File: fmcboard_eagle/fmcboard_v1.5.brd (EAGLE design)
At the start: 147 x 74 mm, 176 parts, among them IC1 OPA699ID, IC10 LTC6229IMS8E#TRPBF, IC11 7805TV, IC12 SN74AUC2G66DCTR, IC13 SN74AUC2G66DCTR, IC14 SN74AUC2G66DCTR, IC15 SN74AUC2G66DCTR, IC16 DAC7578SPWR, IC17 SN74AUC2G66DCTR, IC18 SN74AUC2G66DCTR, IC19 SN74AUC2G66DCTR, IC2 DAC7578SPWR, IC20 SN74AUC2G66DCTR, IC21 74AUP2GU04GW,125, IC22 74AUP2GU04GW,125, IC23 74AUP2GU04GW,125, IC24 74AUP2GU04GW,125, IC25 LM358, IC3 LTC6229IMS8E#TRPBF, IC4 LTC6229IMS8E#TRPBF, IC6 OPA699ID, IC7 OPA699ID, IC8 LTC6229IMS8E#TRPBF, IC9 LTC6229IMS8E#TRPBF, J1 8pin, J10 8pin, J12 4p-2.54, J2 ASP-134604-01, J3 4p-2.54, J4 4p-2.54, J5 8pin, J6 4p-2.54, J7 4p-2.54, J8 4p-2.54, J9 8pin, U1 TXS0108EPWR, U2 STMICROELECTRONICS_L7905ACVST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

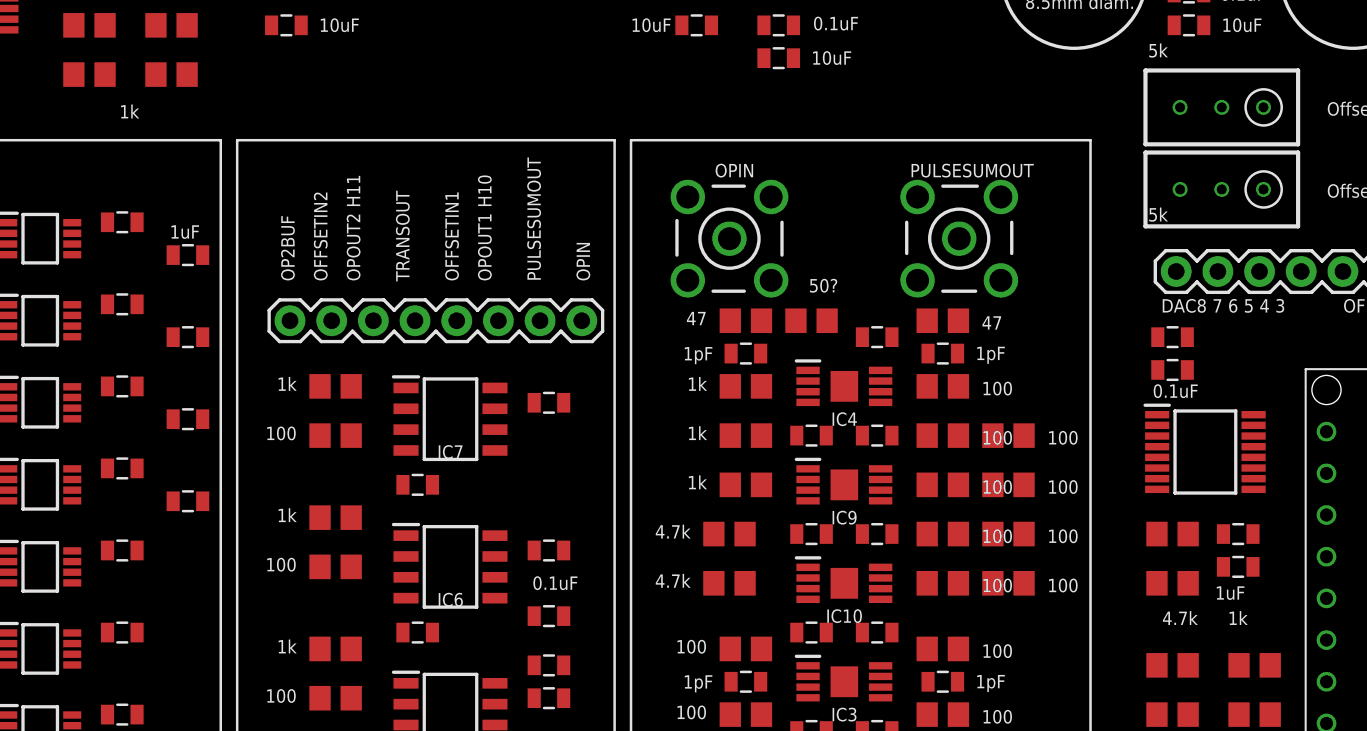
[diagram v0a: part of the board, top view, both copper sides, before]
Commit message: 100 ohm between dac and caps
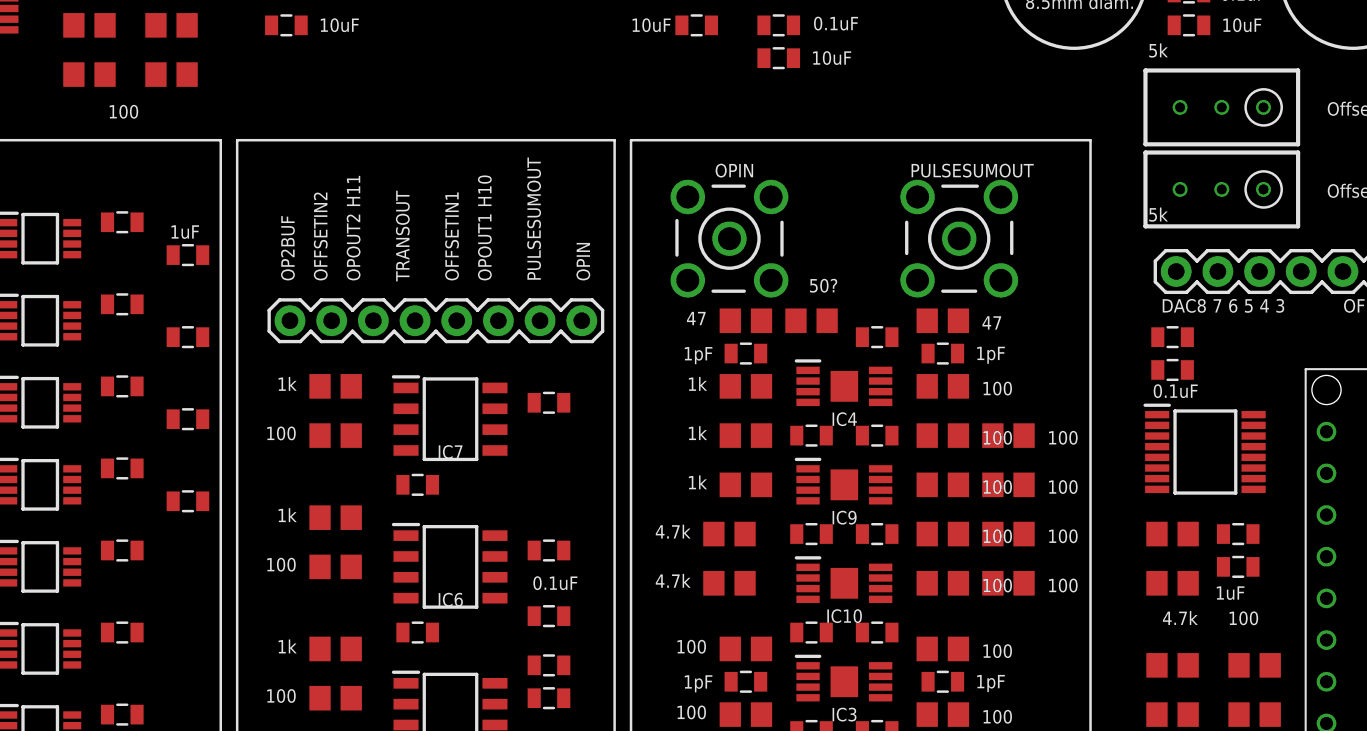
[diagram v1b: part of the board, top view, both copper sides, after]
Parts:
- R47, R53, R54, R55, R56, R57, R58, R59, R60, R61: value 1k -> 100
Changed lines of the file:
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@@
 <attribute name="VALUE" x="107" y="3.19" size="0.8128" layer="21" align="bottom-center"/>
 </element>
-<element name="R47" library="rcl" library_urn="urn:adsk.eagle:library:334" package="R0805" package3d_urn="urn:adsk.eagle:package:23553/2" value="1k" x="54" y="72" smashed="yes">
+<element name="R47" library="rcl" library_urn="urn:adsk.eagle:library:334" package="R0805" package3d_urn="urn:adsk.eagle:package:23553/2" value="100" x="54" y="72" smashed="yes">
 <attribute name="POPULARITY" value="85" x="54" y="72" size="1.778" layer="27" display="off"/>
 <attribute name="SPICEPREFIX" value="R" x="54" y="72" size="1.778" layer="27" display="off"/>
 </element>
-<element name="R53" library="rcl" library_urn="urn:adsk.eagle:library:334" package="R0805" package3d_urn="urn:adsk.eagle:package:23553/2" value="1k" x="54" y="66" smashed="yes">
+<element name="R53" library="rcl" library_urn="urn:adsk.eagle:library:334" package="R0805" package3d_urn="urn:adsk.eagle:package:23553/2" value="100" x="54" y="66" smashed="yes">
 <attribute name="POPULARITY" value="85" x="54" y="66" size="1.778" layer="27" display="off"/>
 <attribute name="SPICEPREFIX" value="R" x="54" y="66" size="1.778" layer="27" display="off"/>
 </element>
-<element name="R54" library="rcl" library_urn="urn:adsk.eagle:library:334" package="R0805" package3d_urn="urn:adsk.eagle:package:23553/2" value="1k" x="59" y="72" smashed="yes">
+<element name="R54" library="rcl" library_urn="urn:adsk.eagle:library:334" package="R0805" package3d_urn="urn:adsk.eagle:package:23553/2" value="100" x="59" y="72" smashed="yes">
 <attribute name="POPULARITY" value="85" x="59" y="72" size="1.778" layer="27" display="off"/>
 <attribute name="SPICEPREFIX" value="R" x="59" y="72" size="1.778" layer="27" display="off"/>
 </element>
-<element name="R55" library="rcl" library_urn="urn:adsk.eagle:library:334" package="R0805" package3d_urn="urn:adsk.eagle:package:23553/2" value="1k" x="59" y="66" smashed="yes">
+<element name="R55" library="rcl" library_urn="urn:adsk.eagle:library:334" package="R0805" package3d_urn="urn:adsk.eagle:package:23553/2" value="100" x="59" y="66" smashed="yes">
 <attribute name="POPULARITY" value="85" x="59" y="66" size="1.778" layer="27" display="off"/>
 <attribute name="SPICEPREFIX" value="R" x="59" y="66" size="1.778" layer="27" display="off"/>
 </element>
-<element name="R56" library="rcl" library_urn="urn:adsk.eagle:library:334" package="R0805" package3d_urn="urn:adsk.eagle:package:23553/2" value="1k" x="54" y="69" smashed="yes" rot="R180">
+<element name="R56" library="rcl" library_urn="urn:adsk.eagle:library:334" package="R0805" package3d_urn="urn:adsk.eagle:package:23553/2" value="100" x="54" y="69" smashed="yes" rot="R180">
 <attribute name="POPULARITY" value="85" x="54" y="69" size="1.778" layer="27" rot="R180" display="off"/>
 <attribute name="SPICEPREFIX" value="R" x="54" y="69" size="1.778" layer="27" rot="R180" display="off"/>
 </element>
-<element name="R57" library="rcl" library_urn="urn:adsk.eagle:library:334" package="R0805" package3d_urn="urn:adsk.eagle:package:23553/2" value="1k" x="54" y="63" smashed="yes" rot="R180">
+<element name="R57" library="rcl" library_urn="urn:adsk.eagle:library:334" package="R0805" package3d_urn="urn:adsk.eagle:package:23553/2" value="100" x="54" y="63" smashed="yes" rot="R180">
 <attribute name="POPULARITY" value="85" x="54" y="63" size="1.778" layer="27" rot="R180" display="off"/>
 <attribute name="SPICEPREFIX" value="R" x="54" y="63" size="1.778" layer="27" rot="R180" display="off"/>
 <attribute name="VALUE" x="57.035" y="61.14" size="0.8128" layer="21" rot="R180"/>
 </element>
-<element name="R58" library="rcl" library_urn="urn:adsk.eagle:library:334" package="R0805" package3d_urn="urn:adsk.eagle:package:23553/2" value="1k" x="59" y="69" smashed="yes" rot="R180">
+<element name="R58" library="rcl" library_urn="urn:adsk.eagle:library:334" package="R0805" package3d_urn="urn:adsk.eagle:package:23553/2" value="100" x="59" y="69" smashed="yes" rot="R180">
 <attribute name="POPULARITY" value="85" x="59" y="69" size="1.778" layer="27" rot="R180" display="off"/>
 <attribute name="SPICEPREFIX" value="R" x="59" y="69" size="1.778" layer="27" rot="R180" display="off"/>
 </element>
-<element name="R59" library="rcl" library_urn="urn:adsk.eagle:library:334" package="R0805" package3d_urn="urn:adsk.eagle:package:23553/2" value="1k" x="59" y="63" smashed="yes" rot="R180">
+<element name="R59" library="rcl" library_urn="urn:adsk.eagle:library:334" package="R0805" package3d_urn="urn:adsk.eagle:package:23553/2" value="100" x="59" y="63" smashed="yes" rot="R180">
 <attribute name="POPULARITY" value="85" x="59" y="63" size="1.778" layer="27" rot="R180" display="off"/>
 <attribute name="SPICEPREFIX" value="R" x="59" y="63" size="1.778" layer="27" rot="R180" display="off"/>
 </element>
-<element name="R60" library="rcl" library_urn="urn:adsk.eagle:library:334" package="R0805" package3d_urn="urn:adsk.eagle:package:23553/2" value="1k" x="125" y="27" smashed="yes">
+<element name="R60" library="rcl" library_urn="urn:adsk.eagle:library:334" package="R0805" package3d_urn="urn:adsk.eagle:package:23553/2" value="100" x="125" y="27" smashed="yes">
 <attribute name="POPULARITY" value="85" x="125" y="27" size="1.778" layer="27" display="off"/>
 <attribute name="SPICEPREFIX" value="R" x="125" y="27" size="1.778" layer="27" display="off"/>
 </element>
-<element name="R61" library="rcl" library_urn="urn:adsk.eagle:library:334" package="R0805" package3d_urn="urn:adsk.eagle:package:23553/2" value="1k" x="125" y="24" smashed="yes" rot="R180">
+<element name="R61" library="rcl" library_urn="urn:adsk.eagle:library:334" package="R0805" package3d_urn="urn:adsk.eagle:package:23553/2" value="100" x="125" y="24" smashed="yes" rot="R180">
 <attribute name="POPULARITY" value="85" x="125" y="24" size="1.778" layer="27" rot="R180" display="off"/>
 <attribute name="SPICEPREFIX" value="R" x="125" y="24" size="1.778" layer="27" rot="R180" display="off"/>

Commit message: routed
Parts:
- removed IO_G2: BU-SMB-V, con-coax:BU-SMB-V
- added IO_C10: BU-SMB-V, con-coax:BU-SMB-V
- added J11: 8pin, SparkFun-Connectors:1X08
- moved IO_H5 36.0 mm to (95.0, 6.00)
- moved R16 36.0 mm to (90.0, 6.00)
- moved R4 36.0 mm to (54.0, 6.00)
- moved J5 7.00 mm to (84.0, 55.0)
- renumbered IO_G3 to IO_H34
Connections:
- removed net G2: IO_G2.1, J2.G2, R4.P$2
- removed net G3: IO_H34.1, J2.G3, R5.P$2
- net C10: now also IO_C10.1, R4.P$2
- net GND: now also IO_C10.2, IO_C10.3, IO_C10.4, IO_C10.5, J11.1, J11.2, J11.3, J11.4, J11.5, J11.6, J11.7, J11.8; no longer IO_G2.2, IO_G2.3, IO_G2.4, IO_G2.5
- net H34: now also IO_H34.1, R5.P$2
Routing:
- net GND: track 1.54 -> 391.2 mm, vias 0 -> 43
- net VS+: track 0.00 -> 347.3 mm, vias 0 -> 12
- net VS-: track 0.00 -> 331.7 mm, vias 0 -> 4
- net 1V8: track 1.94 -> 266.6 mm, vias 0 -> 5
- net VL: track 0.00 -> 213.0 mm, vias 0 -> 4
- net AR_SDAIN2: track 0.00 -> 180.6 mm, vias 0 -> 4
- net C10: track 0.93 -> 175.4 mm, vias 0 -> 3
- net G37: track 0.96 -> 163.2 mm, vias 0 -> 2
- net G36: track 0.94 -> 161.7 mm, vias 0 -> 5
- net VH: track 0.00 -> 148.0 mm, vias 0 -> 4
- net AR_SCLIN2: track 0.00 -> 140.0 mm, vias 0 -> 5
- net OPOUT1_H10: track 0.81 -> 128.7 mm, vias 0 -> 6
- net H34: track 0.82 -> 127.2 mm, vias 0 -> 4
- net SDAIN: track 0.96 -> 125.6 mm, vias 0 -> 3
- net SCLIN: track 0.96 -> 124.3 mm, vias 0 -> 3
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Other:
- board text added: "GNDs"

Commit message: v1.51
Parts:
- C32, C33: value 1pF -> 1pF?
- IC21, IC22, IC23, IC24: value 74AUP2GU04GW,125 -> 74AUP2GU04GW
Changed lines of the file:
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@@
 <layer number="14" name="Route14" color="1" fill="6" visible="no" active="no"/>
 <layer number="15" name="route" color="19" fill="1" visible="yes" active="yes"/>
-<layer number="16" name="gnd" color="1" fill="1" visible="yes" active="yes"/>
+<layer number="16" name="gnd" color="1" fill="1" visible="no" active="yes"/>
 <layer number="17" name="Pads" color="2" fill="1" visible="yes" active="yes"/>
 <layer number="18" name="Vias" color="2" fill="1" visible="yes" active="yes"/>
@@
 <attribute name="VALUE" x="107.984" y="18.603" size="0.8128" layer="21"/>
 </element>
-<element name="C32" library="SparkFun-Passives" package="0805" value="1pF" x="106" y="46" smashed="yes" rot="R180">
+<element name="C32" library="SparkFun-Passives" package="0805" value="1pF?" x="106" y="46" smashed="yes" rot="R180">
+<attribute name="DNP" value="" x="106" y="46" size="1.778" layer="27" rot="R180" display="off"/>
 <attribute name="VALUE" x="107.984" y="45.603" size="0.8128" layer="21"/>
 </element>
-<element name="C33" library="SparkFun-Passives" package="0805" value="1pF" x="94" y="46" smashed="yes" rot="R180">
+<element name="C33" library="SparkFun-Passives" package="0805" value="1pF?" x="94" y="46" smashed="yes" rot="R180">
+<attribute name="DNP" value="" x="94" y="46" size="1.778" layer="27" rot="R180" display="off"/>
 <attribute name="VALUE" x="92.016" y="46.397" size="0.8128" layer="21" rot="R180"/>
 </element>
@@
 <attribute name="MOUSER_PRICE-STOCK" value="https://www.mouser.co.uk/ProductDetail/Texas-Instruments/SN74AUC2G66DCTR?qs=X3IDIfI%252BJAXYLrXiJRkcqA%3D%3D" x="31" y="18" size="0.8128" layer="27" display="off"/>
 </element>
-<element name="IC21" library="74AUP2GU04GW_125" package="SOT65P210X110-6N" value="74AUP2GU04GW,125" x="41" y="53" smashed="yes">
+<element name="IC21" library="74AUP2GU04GW_125" package="SOT65P210X110-6N" value="74AUP2GU04GW" x="41" y="53" smashed="yes">
 <attribute name="DESCRIPTION" value="Inverters DUAL UNBUFF INVERTER 1.8V" x="41" y="53" size="0.8128" layer="27" display="off"/>
 <attribute name="HEIGHT" value="1.1mm" x="41" y="53" size="0.8128" layer="27" display="off"/>
+<attribute name="JLC_ROTATION" value="270" x="41" y="53" size="1.778" layer="27" display="off"/>
 <attribute name="MANUFACTURER_NAME" value="Nexperia" x="41" y="53" size="0.8128" layer="27" display="off"/>
-<attribute name="MANUFACTURER_PART_NUMBER" value="74AUP2GU04GW,125" x="41" y="53" size="0.8128" layer="27" display="off"/>
+<attribute name="MANUFACTURER_PART_NUMBER" value="74AUP2GU04GW" x="41" y="53" size="0.8128" layer="27" display="off"/>
 <attribute name="MOUSER_PART_NUMBER" value="771-74AUP2GU04GW-G" x="41" y="53" size="0.8128" layer="27" display="off"/>
 <attribute name="MOUSER_PRICE-STOCK" value="https://www.mouser.com/Search/Refine.aspx?Keyword=771-74AUP2GU04GW-G" x="41" y="53" size="0.8128" layer="27" display="off"/>
@@
 <attribute name="VALUE" x="38" y="49" size="0.8128" layer="21" rot="R90" align="center"/>
 </element>
-<element name="IC22" library="74AUP2GU04GW_125" package="SOT65P210X110-6N" value="74AUP2GU04GW,125" x="41" y="43" smashed="yes">
+<element name="IC22" library="74AUP2GU04GW_125" package="SOT65P210X110-6N" value="74AUP2GU04GW" x="41" y="43" smashed="yes">
 <attribute name="DESCRIPTION" value="Inverters DUAL UNBUFF INVERTER 1.8V" x="41" y="43" size="0.8128" layer="27" display="off"/>
 <attribute name="HEIGHT" value="1.1mm" x="41" y="43" size="0.8128" layer="27" display="off"/>
+<attribute name="JLC_ROTATION" value="270" x="41" y="43" size="1.778" layer="27" display="off"/>
 <attribute name="MANUFACTURER_NAME" value="Nexperia" x="41" y="43" size="0.8128" layer="27" display="off"/>
-<attribute name="MANUFACTURER_PART_NUMBER" value="74AUP2GU04GW,125" x="41" y="43" size="0.8128" layer="27" display="off"/>
+<attribute name="MANUFACTURER_PART_NUMBER" value="74AUP2GU04GW" x="41" y="43" size="0.8128" layer="27" display="off"/>
 <attribute name="MOUSER_PART_NUMBER" value="771-74AUP2GU04GW-G" x="41" y="43" size="0.8128" layer="27" display="off"/>
 <attribute name="MOUSER_PRICE-STOCK" value="https://www.mouser.com/Search/Refine.aspx?Keyword=771-74AUP2GU04GW-G" x="41" y="43" size="0.8128" layer="27" display="off"/>
 </element>
-<element name="IC23" library="74AUP2GU04GW_125" package="SOT65P210X110-6N" value="74AUP2GU04GW,125" x="41" y="48" smashed="yes">
+<element name="IC23" library="74AUP2GU04GW_125" package="SOT65P210X110-6N" value="74AUP2GU04GW" x="41" y="48" smashed="yes">
 <attribute name="DESCRIPTION" value="Inverters DUAL UNBUFF INVERTER 1.8V" x="41" y="48" size="0.8128" layer="27" display="off"/>
 <attribute name="HEIGHT" value="1.1mm" x="41" y="48" size="0.8128" layer="27" display="off"/>
+<attribute name="JLC_ROTATION" value="270" x="41" y="48" size="1.778" layer="27" display="off"/>
 <attribute name="MANUFACTURER_NAME" value="Nexperia" x="41" y="48" size="0.8128" layer="27" display="off"/>
-<attribute name="MANUFACTURER_PART_NUMBER" value="74AUP2GU04GW,125" x="41" y="48" size="0.8128" layer="27" display="off"/>
+<attribute name="MANUFACTURER_PART_NUMBER" value="74AUP2GU04GW" x="41" y="48" size="0.8128" layer="27" display="off"/>
 <attribute name="MOUSER_PART_NUMBER" value="771-74AUP2GU04GW-G" x="41" y="48" size="0.8128" layer="27" display="off"/>
 <attribute name="MOUSER_PRICE-STOCK" value="https://www.mouser.com/Search/Refine.aspx?Keyword=771-74AUP2GU04GW-G" x="41" y="48" size="0.8128" layer="27" display="off"/>
 </element>
-<element name="IC24" library="74AUP2GU04GW_125" package="SOT65P210X110-6N" value="74AUP2GU04GW,125" x="41" y="38" smashed="yes">
+<element name="IC24" library="74AUP2GU04GW_125" package="SOT65P210X110-6N" value="74AUP2GU04GW" x="41" y="38" smashed="yes">
 <attribute name="DESCRIPTION" value="Inverters DUAL UNBUFF INVERTER 1.8V" x="41" y="38" size="0.8128" layer="27" display="off"/>
 <attribute name="HEIGHT" value="1.1mm" x="41" y="38" size="0.8128" layer="27" display="off"/>
+<attribute name="JLC_ROTATION" value="270" x="41" y="38" size="1.778" layer="27" display="off"/>
 <attribute name="MANUFACTURER_NAME" value="Nexperia" x="41" y="38" size="0.8128" layer="27" display="off"/>
-<attribute name="MANUFACTURER_PART_NUMBER" value="74AUP2GU04GW,125" x="41" y="38" size="0.8128" layer="27" display="off"/>
+<attribute name="MANUFACTURER_PART_NUMBER" value="74AUP2GU04GW" x="41" y="38" size="0.8128" layer="27" display="off"/>
 <attribute name="MOUSER_PART_NUMBER" value="771-74AUP2GU04GW-G" x="41" y="38" size="0.8128" layer="27" display="off"/>
 <attribute name="MOUSER_PRICE-STOCK" value="https://www.mouser.com/Search/Refine.aspx?Keyword=771-74AUP2GU04GW-G" x="41" y="38" size="0.8128" layer="27" display="off"/>
